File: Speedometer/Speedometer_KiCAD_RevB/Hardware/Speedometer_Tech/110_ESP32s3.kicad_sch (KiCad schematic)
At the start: 26 parts, among them P1100 TYPEC-300D-BCP16H100, P1101 5-146130-2, P1102 M20-8770442R, P1103 5-146130-2, P1104 HTSS-105-01-L-DV, Q1103 DTC123JET1G, Q1104 DTC123JET1G, U1100 ESP32WroomS3

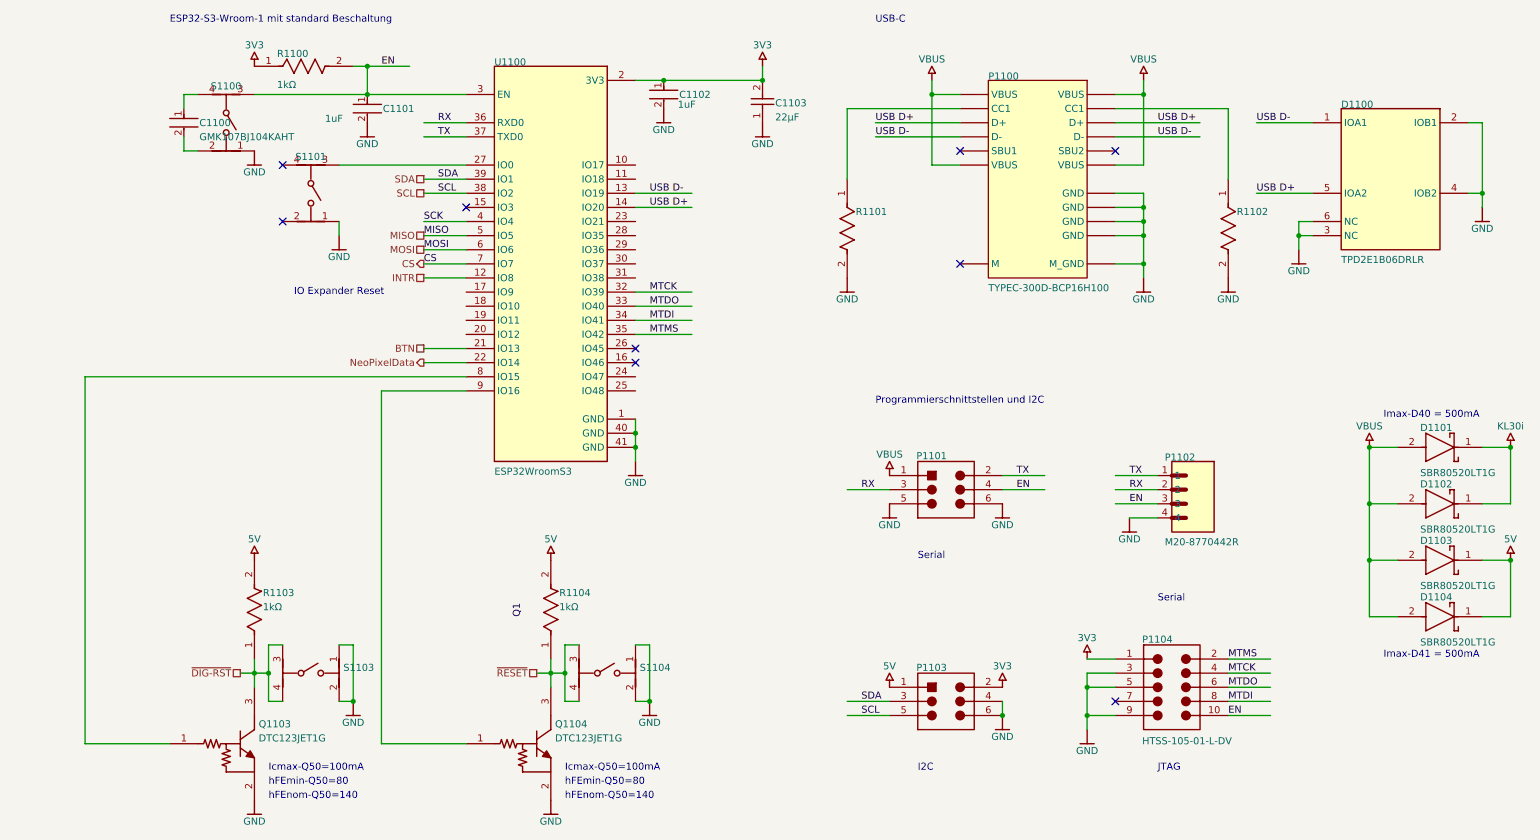
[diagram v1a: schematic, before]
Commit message: current version of lada speedometer in kicad
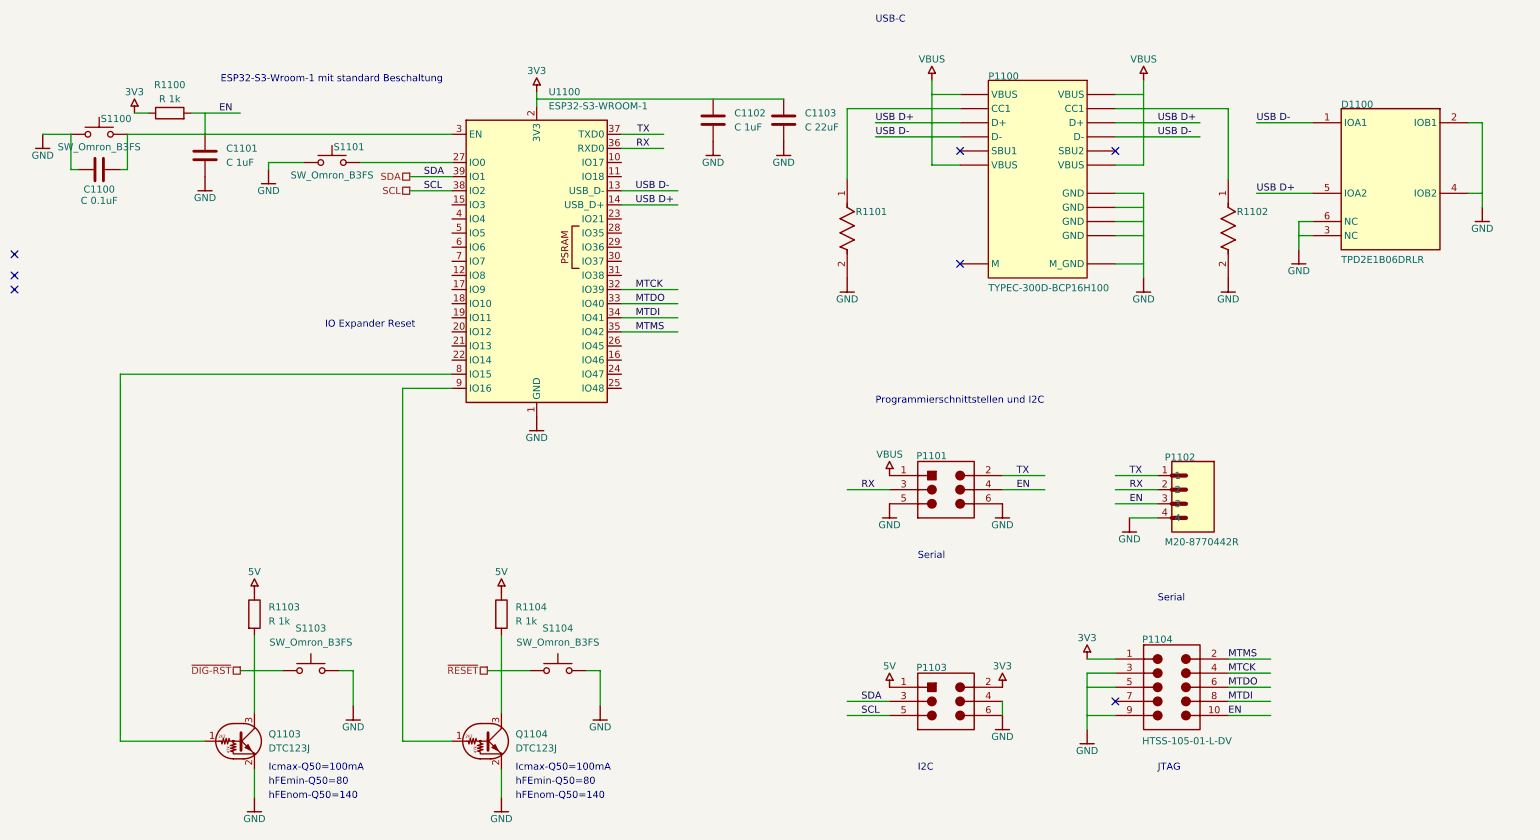
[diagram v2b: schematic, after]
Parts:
- removed C1100: GMK107BJ104KAHT, FP-0603-L_1_6_0_1-W_0_8_0-IPC_B, symbol Speedometer_Tech-altium-import:Designator_0_02cd4be3c70576c341d710602a673aa
- removed C1101, C1102: 1uF, FP-CGA3E-0_3-0_1-MFG, symbol Speedometer_Tech-altium-import:Designator_0_b4654b650e69147ec39a6b967a45e02
- removed C1103: Capacitor 22µF +/-40% 16V 0805, CAPC0805(2012)145_L, symbol Speedometer_Tech-altium-import:Designator_1_CAP-NP-2
- removed D1101, D1102, D1103, D1104: SBR80520LT1G, FP-425-04-MFG, symbol Speedometer_Tech-altium-import:Designator_0_1d6ec82d83fb6aee721767c19dac4b9
- removed Q1103, Q1104: DTC123JET1G, ONSC-SC-75-3-463-01_V, symbol Speedometer_Tech-altium-import:Designator_0_ONSC-BRT-NPN-B1E2C3-3
- removed R1100: 1kΩ, FP-CRCW0603-e3-MFG, symbol Speedometer_Tech-altium-import:Designator_0_1029c3af85768c4190bb7ad29bc67b5
- removed R1103, R1104: 1kΩ, FP-CRCW0603-e3-MFG, symbol Speedometer_Tech-altium-import:Designator_1_1029c3af85768c4190bb7ad29bc67b5
- removed S1100, S1101: ~, FP-PTS645SM43SMTR92LFS-MFG, symbol Speedometer_Tech-altium-import:Designator_3_1adf0dd01260c80cf25a44bfd6b99ba
- removed S1103, S1104: ~, FP-PTS645SM43SMTR92LFS-MFG, symbol Speedometer_Tech-altium-import:Designator_0_1adf0dd01260c80cf25a44bfd6b99ba
- removed U1100: ESP32WroomS3, ESP32WroomS3, symbol Speedometer_Tech-altium-import:Designator_0_ESP32WroomS3
- added C1100: C 0.1uF, Capacitor_SMD:C_0201_0603Metric, symbol Device:C
- added C1101, C1102: C 1uF, Capacitor_SMD:C_0201_0603Metric, symbol Device:C
- added C1103: C 22uF, Capacitor_SMD:C_0805_2012Metric, symbol Device:C
- added Q1103, Q1104: DTC123J, symbol Transistor_BJT:DTC123J
- added R1100, R1103, R1104: R 1k, Resistor_SMD:R_0201_0603Metric, symbol Device:R
- added S1100, S1101, S1103, S1104: SW_Omron_B3FS, Button_Switch_SMD:SW_SPST_Omron_B3FS-100xP, symbol Switch:SW_Omron_B3FS
- added U1100: ESP32-S3-WROOM-1, RF_Module:ESP32-S3-WROOM-1, symbol RF_Module:ESP32-S3-WROOM-1
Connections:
- net 3V3: now also R1100.1, U1100.2 (3V3)
- net 5V: now also R1103.1, R1104.1
- net EN: now also R1100.2
- net GND: now also C1100.2, C1101.2, C1102.2, C1103.2, Q1103.2 (E), Q1104.2 (E), S1100.1, S1101.1, S1103.2, S1104.2, U1100.1 (GND), U1100.40 (GND), U1100.41 (GND); no longer D1100.3 (NC), D1100.4 (IOB2), P1100.A12 (GND), P1100.B1 (GND), P1100.B12 (GND), P1100.M_GND, P1104.5, P1104.9
- net MTCK: now also U1100.32 (IO39)
- net MTDI: now also U1100.34 (IO41)
- net MTDO: now also U1100.33 (IO40)
- net MTMS: now also U1100.35 (IO42)
- net RX: now also U1100.36 (RXD0)
- net SCL: now also U1100.38 (IO2)
- net SDA: now also U1100.39 (IO1)
- net TX: now also U1100.37 (TXD0)
- net USB D+: now also U1100.14 (USB_D+)
- net USB D-: now also U1100.13 (USB_D-)
- net VBUS: no longer P1100.A4 (VBUS), P1100.B4 (VBUS)
- net ~{DIG-RST}: now also S1103.1
- net ~{RESET}: now also S1104.1
- new net: C1100.1, S1100.2, U1100.3 (EN)
- new net: Q1104.1 (B), U1100.9 (IO16)
- new net: Q1104.3 (C), R1104.2
- new net: Q1103.1 (B), U1100.8 (IO15)
- new net: Q1103.3 (C), R1103.2
- new net: S1101.2, U1100.27 (IO0)
- no-connect marks 9 -> 7
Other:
- note removed: "Imax-D40 = 500mA"
- note removed: "Imax-D41 = 500mA"
